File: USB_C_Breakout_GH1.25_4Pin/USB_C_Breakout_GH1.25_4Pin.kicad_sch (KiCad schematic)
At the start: 7 parts, among them J1 USB_C_Receptacle_USB2.0, J2 Conn_01x04_MountingPin

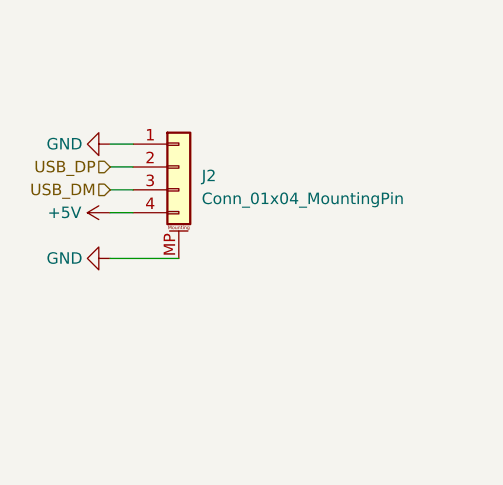
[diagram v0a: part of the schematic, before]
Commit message: change USB pin sequence to make it more universal
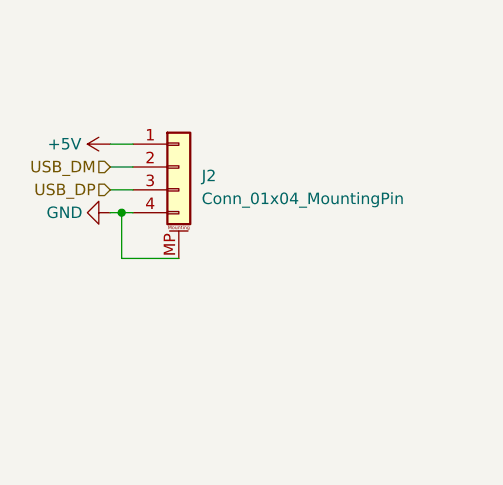
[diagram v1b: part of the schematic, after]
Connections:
- net +5V: now also J2.1 (Pin_1); no longer J2.4 (Pin_4)
- net GND: now also J2.4 (Pin_4); no longer J2.1 (Pin_1)
- net USB_DM: now also J2.2 (Pin_2); no longer J2.3 (Pin_3)
- net USB_DP: now also J2.3 (Pin_3); no longer J2.2 (Pin_2)
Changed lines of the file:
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@@
   (junction (at 209.55 119.38) (diameter 0) (color 0 0 0 0)
+  )
+  (junction (at 105.41 93.98) (diameter 0) (color 0 0 0 0)
   )
   (junction (at 182.88 78.74) (diameter 0) (color 0 0 0 0)
@@
     (stroke (width 0) (type default))
   )
+  (wire (pts (xy 105.41 99.06) (xy 105.41 93.98))
+    (stroke (width 0) (type default))
+  )
   (wire (pts (xy 200.66 119.38) (xy 200.66 118.11))
     (stroke (width 0) (type default))
@@
     (stroke (width 0) (type default))
   )
-  (wire (pts (xy 104.14 91.44) (xy 106.68 91.44))
+  (wire (pts (xy 104.14 88.9) (xy 106.68 88.9))
     (stroke (width 0) (type default))
   )
-  (wire (pts (xy 104.14 93.98) (xy 106.68 93.98))
+  (wire (pts (xy 111.76 99.06) (xy 105.41 99.06))
+    (stroke (width 0) (type default))
+  )
+  (wire (pts (xy 104.14 86.36) (xy 106.68 86.36))
     (stroke (width 0) (type default))
   )
@@
     (stroke (width 0) (type default))
   )
-  (wire (pts (xy 104.14 86.36) (xy 106.68 86.36))
+  (wire (pts (xy 104.14 93.98) (xy 105.41 93.98))
     (stroke (width 0) (type default))
   )
@@
     (stroke (width 0) (type default))
   )
-  (wire (pts (xy 104.14 88.9) (xy 106.68 88.9))
+  (wire (pts (xy 104.14 91.44) (xy 106.68 91.44))
     (stroke (width 0) (type default))
   )
@@
     (stroke (width 0) (type default))
   )
-  (wire (pts (xy 104.14 99.06) (xy 111.76 99.06))
+  (wire (pts (xy 105.41 93.98) (xy 106.68 93.98))
     (stroke (width 0) (type default))
   )
@@
     (stroke (width 0) (type default))
   )
-  (hierarchical_label "USB_DP" (shape input) (at 104.14 88.9 180) (fields_autoplaced)
+  (hierarchical_label "USB_DP" (shape input) (at 104.14 91.44 180) (fields_autoplaced)
     (effects (font (size 1.27 1.27)) (justify right))
   )
@@
     (effects (font (size 1.27 1.27)) (justify right))
   )
-  (hierarchical_label "USB_DM" (shape input) (at 104.14 91.44 180) (fields_autoplaced)
+  (hierarchical_label "USB_DM" (shape input) (at 104.14 88.9 180) (fields_autoplaced)
     (effects (font (size 1.27 1.27)) (justify right))
   )
@@
     (effects (font (size 1.27 1.27)) (justify right))
   )
-  (symbol (lib_id "power:GND") (at 104.14 86.36 270) (unit 1)
+  (symbol (lib_id "power:GND") (at 104.14 93.98 270) (mirror x) (unit 1)
     (in_bom yes) (on_board yes) (dnp no)
-    (property "Reference" "#PWR08" (at 97.79 86.36 0)
+    (property "Reference" "#PWR08" (at 97.79 93.98 0)
       (effects (font (size 1.27 1.27)) hide)
     )
-    (property "Value" "GND" (at 99.06 86.36 90)
+    (property "Value" "GND" (at 99.06 93.98 90)
       (effects (font (size 1.27 1.27)))
     )
-    (property "Footprint" "" (at 104.14 86.36 0)
+    (property "Footprint" "" (at 104.14 93.98 0)
       (effects (font (size 1.27 1.27)) hide)
     )
-    (property "Datasheet" "" (at 104.14 86.36 0)
+    (property "Datasheet" "" (at 104.14 93.98 0)
       (effects (font (size 1.27 1.27)) hide)
     )
@@
     )
   )
-  (symbol (lib_id "power:GND") (at 104.14 99.06 270) (unit 1)
+  (symbol (lib_id "power:+5V") (at 104.14 86.36 90) (mirror x) (unit 1)
     (in_bom yes) (on_board yes) (dnp no)
-    (property "Reference" "#PWR08" (at 97.79 99.06 0)
+    (property "Reference" "#PWR01" (at 107.95 86.36 0)
       (effects (font (size 1.27 1.27)) hide)
     )
-    (property "Value" "GND" (at 99.06 99.06 90)
+    (property "Value" "+5V" (at 99.06 86.36 90)
       (effects (font (size 1.27 1.27)))
     )
-    (property "Footprint" "" (at 104.14 99.06 0)
+    (property "Footprint" "" (at 104.14 86.36 0)
       (effects (font (size 1.27 1.27)) hide)
     )
-    (property "Datasheet" "" (at 104.14 99.06 0)
+    (property "Datasheet" "" (at 104.14 86.36 0)
       (effects (font (size 1.27 1.27)) hide)
     )
-    (pin "1")
-    (instances
-      (project "ESP32C3_RF_Test"
-        (path "/69af12a2-5232-4c58-9eb8-e4dda022defa"
-          (reference "#PWR08") (unit 1)
-        )
-      )
-      (project "USB_C_Breakout_GH1.25_4Pin"
-        (path "/ad332f2e-806d-450e-8cd7-d542be9fc8cd"
-          (reference "#PWR06") (unit 1)
-        )
-      )
-      (project "RotaryPositionEncoder_RP2040"
-        (path "/f25ab52f-01ff-41aa-888b-6209c4e1870f"
-          (reference "#PWR017") (unit 1)
-        )
-      )
-    )
-  )
-  (symbol (lib_id "power:+5V") (at 104.14 93.98 90) (unit 1)
-    (in_bom yes) (on_board yes) (dnp no)
-    (property "Reference" "#PWR01" (at 107.95 93.98 0)
-      (effects (font (size 1.27 1.27)) hide)
-    )
-    (property "Value" "+5V" (at 99.06 93.98 90)
-      (effects (font (size 1.27 1.27)))
-    )
-    (property "Footprint" "" (at 104.14 93.98 0)
-      (effects (font (size 1.27 1.27)) hide)
-    )
-    (property "Datasheet" "" (at 104.14 93.98 0)
-      (effects (font (size 1.27 1.27)) hide)
-    )
